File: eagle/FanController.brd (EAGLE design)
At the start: 45 x 20 mm, 17 parts, among them IC102 LDK320AM33R, IC201 STM32F042G6U6, IC202 MAX6002EUR+T, Q302 BSS123

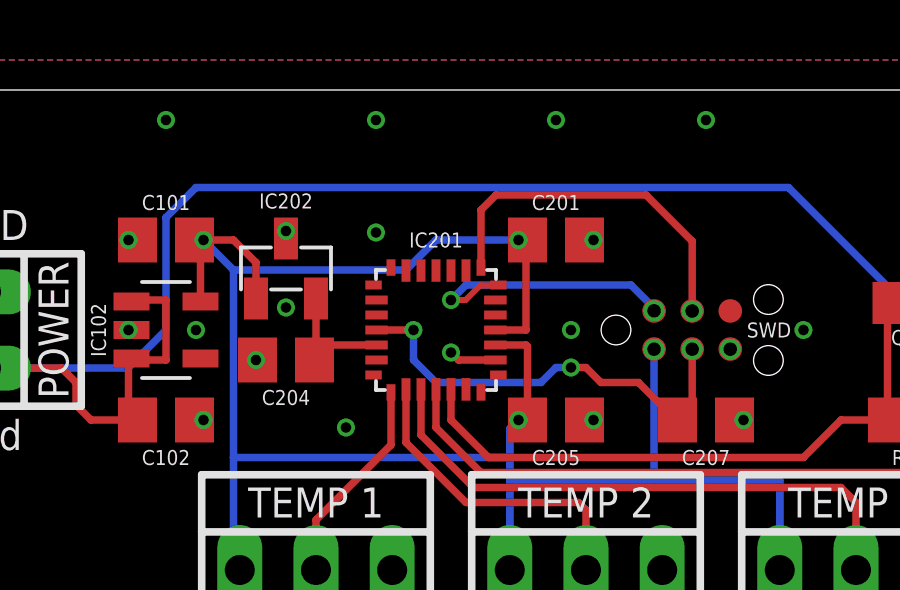
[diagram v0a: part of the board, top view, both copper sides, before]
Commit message: - removed 2V5 voltage reference since it is useless
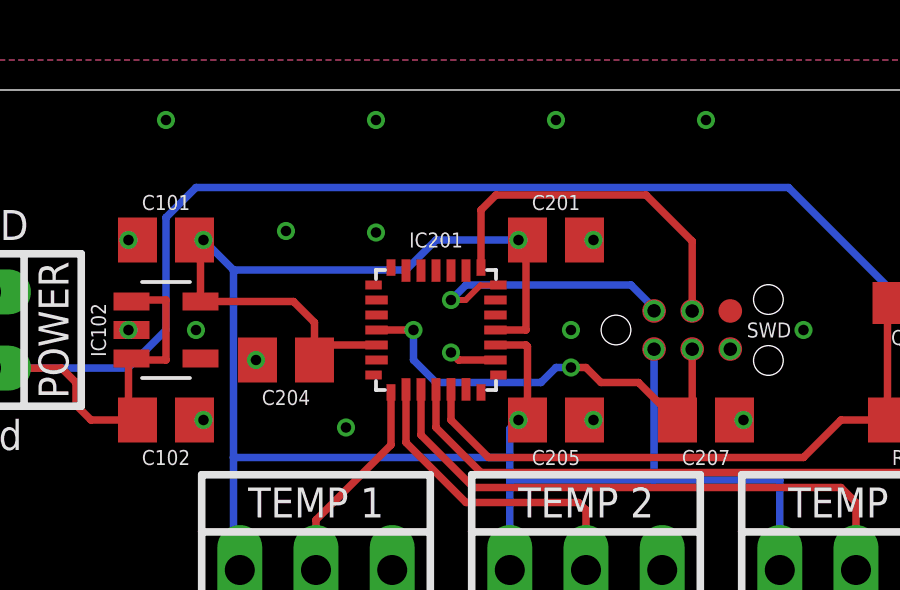
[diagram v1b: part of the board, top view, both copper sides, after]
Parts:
- removed IC202: MAX6002EUR+T, MAX600X - Voltage Reference:SOT23-3
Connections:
- removed net STM32:VCCA: C204.2, IC201.5_VDDA, IC202.2_OUT
- net 3V3: now also C204.2, IC201.5_VDDA; no longer IC202.1_IN
- net GND: no longer IC202.3_GND
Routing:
- net STM32:VCCA: track 4.35 -> 0.00 mm
- net 3V3: track 66.3 -> 70.4 mm
- net GND: vias 38 -> 37
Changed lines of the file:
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@@
 <attribute name="VALUE" x="19.25" y="8.75" size="0.5" layer="27" font="vector" align="center"/>
-</element>
-<element name="IC202" library="MAX600X - Voltage Reference" package="SOT23-3" value="MAX6002EUR+T" x="14" y="14.05" smashed="yes">
-<attribute name="NAME" x="14" y="16.3" size="0.5" layer="25" font="vector" align="center"/>
-<attribute name="VALUE" x="14" y="14.05" size="0.5" layer="27" font="vector" rot="R270" align="center"/>
 </element>
 <element name="SWD101" library="tag-connect" package="TC2030-NL" value="TC2030-NL" x="25" y="12" smashed="yes">
@@
 <contactref element="C201" pad="1"/>
 <contactref element="C205" pad="1"/>
-<contactref element="IC202" pad="3_GND"/>
 <contactref element="IC201" pad="16_VSS"/>
 <contactref element="TEMP400" pad="3"/>
@@
 <via x="31.25" y="12" extent="1-16" drill="0.35"/>
 <via x="11" y="12" extent="1-16" drill="0.35"/>
-<via x="14" y="12.75" extent="1-16" drill="0.35"/>
 </signal>
 <signal name="3V3" class="4">
@@
 <contactref element="C201" pad="2"/>
 <contactref element="C205" pad="2"/>
-<contactref element="IC202" pad="1_IN"/>
 <contactref element="IC201" pad="17_VDD"/>
 <contactref element="IC201" pad="18_VDDIO2"/>
@@
 <wire x1="18" y1="14" x2="12.25" y2="14" width="0.25" layer="16"/>
 <wire x1="22.05" y1="9" x2="21.75" y2="9" width="0.25" layer="1"/>
-<wire x1="26.27" y1="11.36" x2="26.5143125" y2="11.36" width="0.25" layer="1"/>
 <wire x1="22.05" y1="15" x2="21.75" y2="15" width="0.25" layer="1"/>
 <wire x1="10.95" y1="15" x2="11.25" y2="15" width="0.25" layer="1"/>
-<wire x1="13" y1="14.25" x2="13" y2="13.05" width="0.25" layer="1"/>
-<wire x1="11.25" y1="15" x2="12.25" y2="15" width="0.25" layer="1"/>
-<wire x1="12.25" y1="15" x2="13" y2="14.25" width="0.25" layer="1"/>
 <wire x1="26.27" y1="7.02" x2="26.25" y2="7" width="0.25" layer="16"/>
 <wire x1="26.27" y1="11.36" x2="26.27" y2="7.02" width="0.25" layer="16"/>
 <wire x1="26.27" y1="11.365" x2="26.27" y2="11.36" width="0.25" layer="1"/>
+<contactref element="IC201" pad="5_VDDA"/>
+<contactref element="C204" pad="2"/>
+<wire x1="11.15" y1="12.95" x2="14.25" y2="12.95" width="0.25" layer="1"/>
+<wire x1="14.95" y1="11" x2="15.45" y2="11.5" width="0.25" layer="1"/>
+<wire x1="15.45" y1="11.5" x2="17.02" y2="11.5" width="0.25" layer="1"/>
+<wire x1="14.95" y1="11" x2="14.95" y2="12.25" width="0.25" layer="1"/>
+<wire x1="14.95" y1="12.25" x2="14.25" y2="12.95" width="0.25" layer="1"/>
 </signal>
 <signal name="SYS_NRST" class="1">
@@
 <wire x1="24.5" y1="10.25" x2="24" y2="10.75" width="0.25" layer="1"/>
 <wire x1="24" y1="10.75" x2="23.5" y2="10.75" width="0.25" layer="1"/>
-<wire x1="27.54" y1="11.36" x2="27.7843125" y2="11.36" width="0.25" layer="1"/>
 <wire x1="27.54" y1="11.365" x2="27.54" y2="11.36" width="0.25" layer="1"/>
 </signal>
@@
 <wire x1="21" y1="16.5" x2="26" y2="16.5" width="0.25" layer="1"/>
 <wire x1="26" y1="16.5" x2="27.54" y2="14.96" width="0.25" layer="1"/>
-<wire x1="27.7839375" y1="12.632" x2="27.539" y2="12.632" width="0.25" layer="1"/>
 <wire x1="27.54" y1="12.635" x2="27.54" y2="14.96" width="0.25" layer="1"/>
 <wire x1="27.54" y1="12.635" x2="27.54" y2="12.633" width="0.25" layer="1"/>
@@
 <wire x1="25.5" y1="13.5" x2="20" y2="13.5" width="0.25" layer="16"/>
 <wire x1="20" y1="13.5" x2="19.5" y2="13" width="0.25" layer="16"/>
-<wire x1="26.27" y1="12.64" x2="26.525684375" y2="12.64" width="0.25" layer="1"/>
 <wire x1="26.27" y1="12.635" x2="26.27" y2="12.64" width="0.25" layer="1"/>
 </signal>
@@
 <wire x1="39" y1="9.46" x2="36.79" y2="7.25" width="0.25" layer="1"/>
 </signal>
-<signal name="STM32:VCCA">
-<contactref element="IC201" pad="5_VDDA"/>
-<contactref element="IC202" pad="2_OUT"/>
-<contactref element="C204" pad="2"/>
-<wire x1="17.02" y1="11.5" x2="15.45" y2="11.5" width="0.25" layer="1"/>
-<wire x1="15.45" y1="11.5" x2="14.95" y2="11" width="0.25" layer="1"/>
-<wire x1="14.95" y1="11" x2="15" y2="11.05" width="0.25" layer="1"/>
-<wire x1="15" y1="11.05" x2="15" y2="13.05" width="0.25" layer="1"/>
-</signal>
 <signal name="FAN:N$1">

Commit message: - commit before rev.2 rev.2 is switch to PWM fans
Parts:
- TEMP400, TEMP500, TEMP600: value 22-23-2031 -> LMT86LPM
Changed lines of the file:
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@@
 <attribute name="VALUE" x="30.75" y="12" size="0.5" layer="27" font="vector" rot="R270" align="center"/>
 </element>
-<element name="TEMP400" library="con-molex" library_urn="urn:adsk.eagle:library:165" package="22-23-2031" package3d_urn="urn:adsk.eagle:package:8078634/1" value="22-23-2031" x="15" y="4" smashed="yes">
+<element name="TEMP400" library="con-molex" library_urn="urn:adsk.eagle:library:165" package="22-23-2031" package3d_urn="urn:adsk.eagle:package:8078634/1" value="LMT86LPM" x="15" y="4" smashed="yes">
 <attribute name="MF" value="MOLEX" x="15" y="4" size="1.778" layer="27" display="off"/>
 <attribute name="MPN" value="22-23-2031" x="15" y="4" size="1.778" layer="27" display="off"/>
@@
 <attribute name="VALUE" x="15" y="4" size="1.016" layer="27" ratio="10"/>
 </element>
-<element name="TEMP500" library="con-molex" library_urn="urn:adsk.eagle:library:165" package="22-23-2031" package3d_urn="urn:adsk.eagle:package:8078634/1" value="22-23-2031" x="24" y="4" smashed="yes">
+<element name="TEMP500" library="con-molex" library_urn="urn:adsk.eagle:library:165" package="22-23-2031" package3d_urn="urn:adsk.eagle:package:8078634/1" value="LMT86LPM" x="24" y="4" smashed="yes">
 <attribute name="MF" value="MOLEX" x="24" y="4" size="1.778" layer="27" display="off"/>
 <attribute name="MPN" value="22-23-2031" x="24" y="4" size="1.778" layer="27" display="off"/>
@@
 <attribute name="VALUE" x="24" y="4" size="1.016" layer="27" ratio="10"/>
 </element>
-<element name="TEMP600" library="con-molex" library_urn="urn:adsk.eagle:library:165" package="22-23-2031" package3d_urn="urn:adsk.eagle:package:8078634/1" value="22-23-2031" x="33" y="4" smashed="yes">
+<element name="TEMP600" library="con-molex" library_urn="urn:adsk.eagle:library:165" package="22-23-2031" package3d_urn="urn:adsk.eagle:package:8078634/1" value="LMT86LPM" x="33" y="4" smashed="yes">
 <attribute name="MF" value="MOLEX" x="33" y="4" size="1.778" layer="27" display="off"/>
 <attribute name="MPN" value="22-23-2031" x="33" y="4" size="1.778" layer="27" display="off"/>

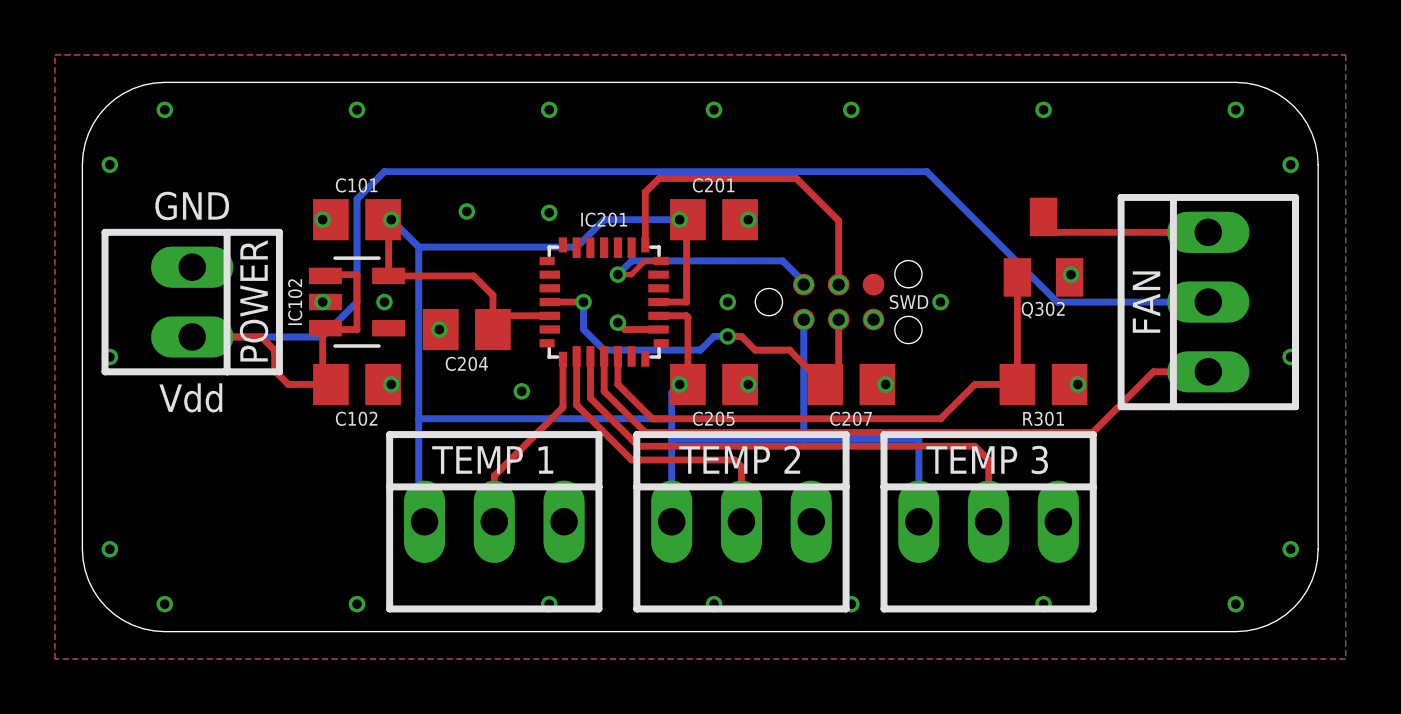
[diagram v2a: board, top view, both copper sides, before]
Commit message: rev.2: PWM fan a PWM fan shall be connected to the controller
- initialized all unused pins as analog
- removed FET for transistor control
- added noctua PWM specification white paper
- rev.2 board marking on tstop
- replaced connectors with pin headers
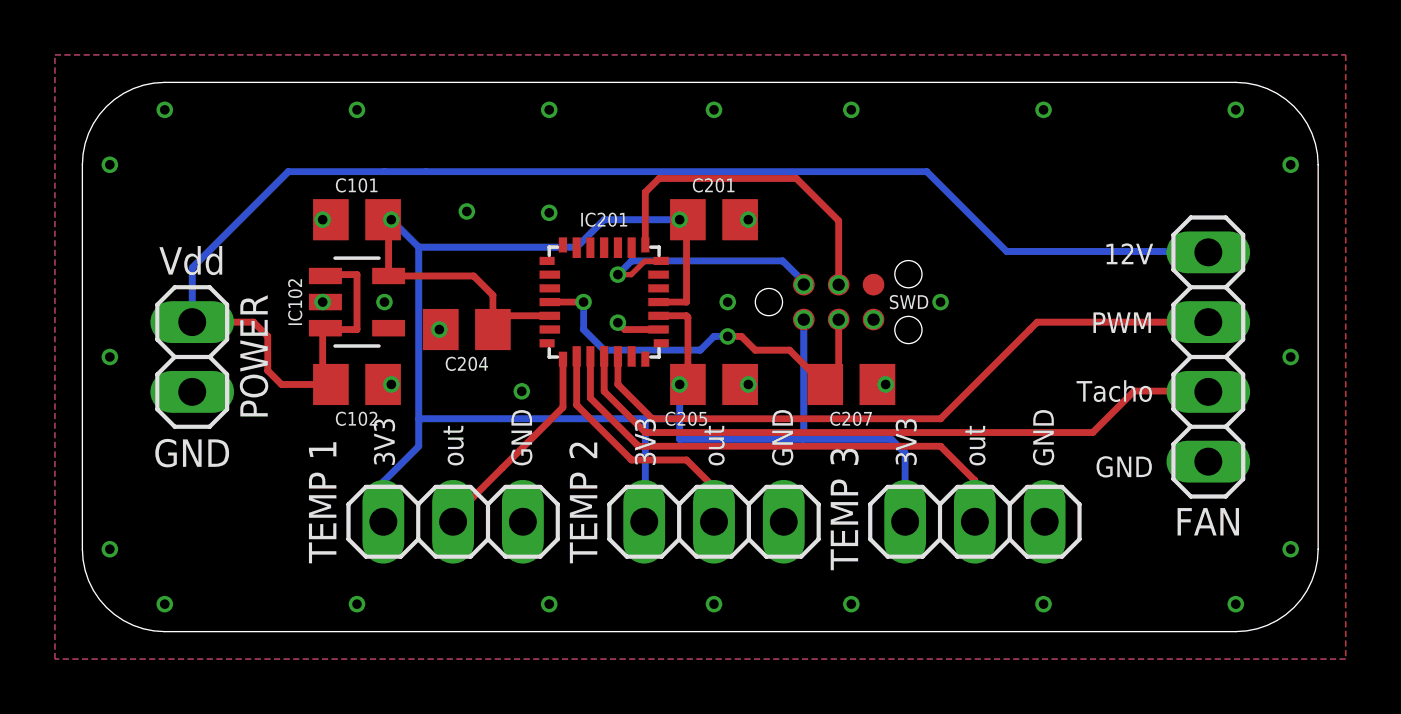
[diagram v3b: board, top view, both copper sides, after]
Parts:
- removed FAN_300: 22-23-2031, con-molex:22-23-2031
- removed Q302: BSS123, transistor-small-signal:SOT23
- removed R301: 10k, rcl:R0805
- added SV301: n/a, pinhead:1X04
- POWER: value 22-23-2021 -> n/a; device con-molex:22-23-2021 -> pinhead:1X02
- TEMP400, TEMP500, TEMP600: device con-molex:22-23-2031 -> pinhead:1X03
- moved POWER 2.00 mm to (4.00, 10.0), turned to 90 degrees
- moved TEMP400 1.50 mm to (13.5, 4.00)
- moved TEMP500 1.00 mm to (23.0, 4.00)
- moved TEMP600 0.50 mm to (32.5, 4.00)
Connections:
- removed net FAN:N$1: FAN_300.3, Q302.3
- net FAN_PWM: now also SV301.3; no longer Q302.1, R301.2
- net FAN_TACHO: now also SV301.2; no longer FAN_300.1
- net GND: now also SV301.1; no longer Q302.2, R301.1
- net VDD: now also SV301.4; no longer FAN_300.2
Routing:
- net FAN:N$1: track 6.56 -> 0.00 mm
- net FAN_PWM: track 20.5 -> 24.5 mm
- net VDD: track 56.5 -> 55.0 mm
- net TEMP2: track 10.7 -> 9.26 mm
- net TEMP3: track 19.2 -> 18.3 mm
- net TEMP1: track 6.96 -> 7.58 mm
- net GND: vias 37 -> 35
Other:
- board text added: "12V"
- board text added: "3V3"
- board text added: "PWM"
- board text added: "Tacho"
- board text added: "ejovrh rev. 2"
- board text added: "out"
- board text removed: "ejovrh rev. 1"

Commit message: - small routing correction
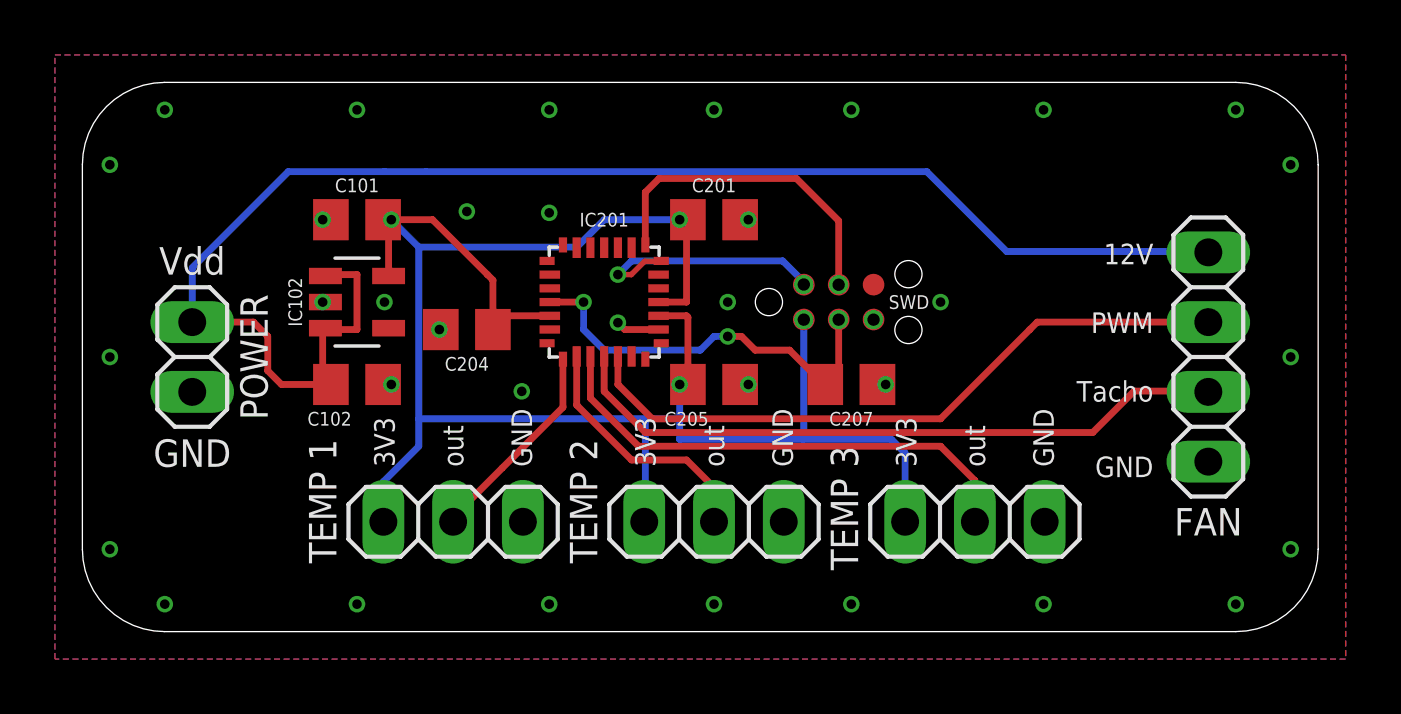
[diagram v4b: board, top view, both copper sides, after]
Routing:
- net 3V3: track 70.7 -> 72.1 mm
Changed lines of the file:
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@@
 </element>
 <element name="C102" library="rcl" library_urn="urn:adsk.eagle:library:334" package="C0805" package3d_urn="urn:adsk.eagle:package:23617/2" value="1μF / 50V" x="10" y="9" smashed="yes">
-<attribute name="NAME" x="10" y="7.75" size="0.5" layer="25" rot="R180" align="center"/>
+<attribute name="NAME" x="9" y="7.75" size="0.5" layer="25" rot="R180" align="center"/>
 <attribute name="POPULARITY" value="88" x="10" y="9" size="1.778" layer="27" display="off"/>
 <attribute name="SPICEPREFIX" value="C" x="10" y="9" size="1.778" layer="27" display="off"/>
@@
 <contactref element="IC201" pad="5_VDDA"/>
 <contactref element="C204" pad="2"/>
-<wire x1="11.15" y1="12.95" x2="14.25" y2="12.95" width="0.25" layer="1"/>
 <wire x1="14.95" y1="11" x2="15.45" y2="11.5" width="0.25" layer="1"/>
 <wire x1="15.45" y1="11.5" x2="17.02" y2="11.5" width="0.25" layer="1"/>
-<wire x1="14.95" y1="11" x2="14.95" y2="12.25" width="0.25" layer="1"/>
-<wire x1="14.95" y1="12.25" x2="14.25" y2="12.95" width="0.25" layer="1"/>
 <contactref element="TEMP400" pad="1"/>
 <contactref element="TEMP500" pad="1"/>
@@
 <wire x1="10.96" y1="4" x2="10.96" y2="5.46" width="0.25" layer="16"/>
 <wire x1="10.96" y1="5.46" x2="12.25" y2="6.75" width="0.25" layer="16"/>
+<wire x1="10.95" y1="15" x2="12.75" y2="15" width="0.25" layer="1"/>
+<wire x1="12.75" y1="15" x2="14.75" y2="13" width="0.25" layer="1"/>
+<wire x1="14.95" y1="11" x2="14.95" y2="12.8" width="0.25" layer="1"/>
+<wire x1="14.95" y1="12.8" x2="14.75" y2="13" width="0.25" layer="1"/>
 </signal>
 <signal name="SYS_NRST" class="1">

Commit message: - coded ADC temperature calculations (timer1) - coded RPM calculations (timer2)
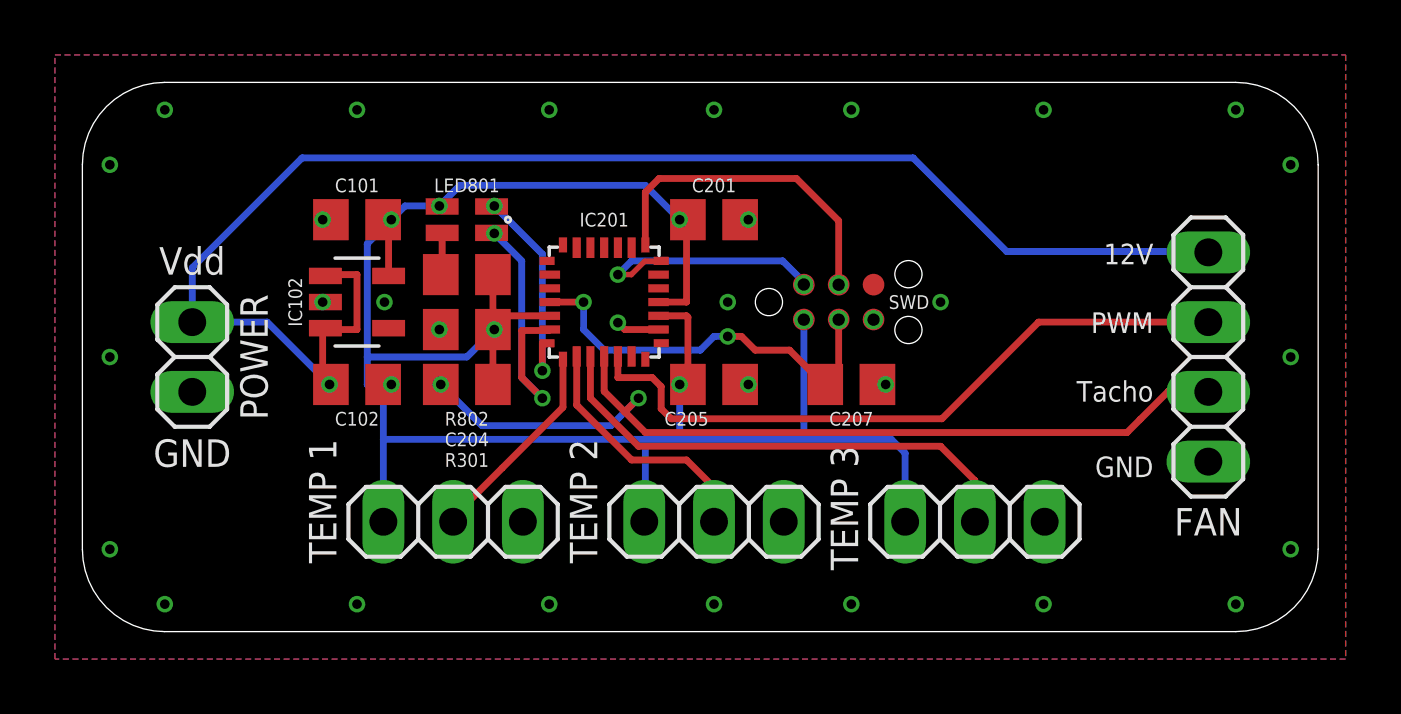
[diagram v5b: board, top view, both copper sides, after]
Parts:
- added LED801: APHBM2012SURKZGKC, APHBM2012LSURKZGKC:SMD
- added R301: 10k, rcl:R0805
- added R802: 68R, rcl:R0805
- renumbered POWER to JP101
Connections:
- new net LED1:R_A: LED801.1, R802.2
- new net LED_GREEN: IC201.7_PA1, LED801.3
- new net LED_RED: IC201.6_PA0, LED801.2
- net 3V3: now also LED801.4, R301.2, R802.1
- net FAN_TACHO: now also R301.1
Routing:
- net LED_RED: track 0.00 -> 10.6 mm, vias 0 -> 2
- net FAN_TACHO: track 24.5 -> 33.5 mm, vias 0 -> 2
- net LED_GREEN: track 0.00 -> 8.00 mm, vias 0 -> 2
- net 3V3: track 72.1 -> 76.4 mm, vias 4 -> 6
- net LED1:R_A: track 0.00 -> 1.54 mm
- net VDD: track 55.0 -> 54.7 mm, vias 0 -> 1
- net GND: vias 35 -> 32
